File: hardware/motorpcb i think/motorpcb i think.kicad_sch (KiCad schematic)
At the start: 0 parts

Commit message: started schematic
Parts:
- added U1: PCA9685PW_Q900_118, symbol motorpcb i think:PCA9685PW_Q900_118

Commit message: continued schematic work
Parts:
- removed U1: PCA9685PW_Q900_118, symbol motorpcb i think:PCA9685PW_Q900_118
- added C1: 100nf, symbol Device:C
- added C2, C5: 10u, symbol Device:C
- added C3: 22u, symbol Device:C
- added C4: 100n, symbol Device:C
- added D1: RED, symbol Device:D
- added D2: GREEN, symbol Device:D
- added D3: BLUE, symbol Device:D
- added J1: USB_C_Receptacle_USB2.0_16P, symbol Connector:USB_C_Receptacle_USB2.0_16P
- added R1, R2, R3, R4, R5, R6: 5.1K, symbol Device:R
- added SW1, SW2: SW_Push, symbol Switch:SW_Push
- added U1: ESP32-S3-WROOM-1-N8, ESP32-S3-WROOM-1-N8:XCVR_ESP32-S3-WROOM-1-N8, symbol motorpcb i think:ESP32-S3-WROOM-1-N8
- added U2: LD1117S33TR, LD1117S33TR:SOT230P700X180-4N, symbol motorpcb i think:LD1117S33TR
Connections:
- new net: J1.A5 (CC1), R2.1
- new net: D1.2 (A), R3.2
- new net: J1.B5 (CC2), R1.1
- new net: D3.2 (A), R5.2
- new net: D2.2 (A), R4.2
- new net +3V3: C2.1, C3.1, C4.1, R4.1, R6.1, U1.2 (3V3), U2.2 (OUT), U2.4 (OUT)
- new net +5V: C1.1, J1.A4 (VBUS), J1.A9 (VBUS), J1.B4 (VBUS), J1.B9 (VBUS), R3.1, U2.3 (IN)
- new net D+: J1.A6 (D+), J1.B6 (D+), U1.14 (IO20)
- new net D-: J1.A7 (D-), J1.B7 (D-), U1.13 (IO19)
- new net GND: C1.2, C2.2, C3.2, C4.2, C5.2, D1.1 (K), D2.1 (K), D3.1 (K), J1.A1 (GND), J1.A12 (GND), J1.B1 (GND), J1.B12 (GND), J1.S1 (SHIELD), R1.2, R2.2, SW1.1, SW2.1, U1.1 (GND), U1.40 (GND), U1.41_1 (GND), U1.41_2 (GND), U1.41_3 (GND), U1.41_4 (GND), U1.41_5 (GND), U1.41_6 (GND), U1.41_7 (GND), U1.41_8 (GND), U1.41_9 (GND), U2.1 (GND)
- new net GPIO0: SW1.2, U1.27 (IO0)
- new net GPIO21: R5.1, U1.23 (IO21)
- new net en: C5.1, R6.2, SW2.2, U1.3 (EN)
- no-connect marks 0 -> 2
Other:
- note added: "boot / reset"
- note added: "esp32 3v3 regulator"
- note added: "indicator LED"
- note added: "usb c connector"

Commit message: finishing up basic esp32s3 hardware
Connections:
- net GPIO17: now reaches U1.10 (IO17)
- net GPIO18: now reaches U1.11 (IO18)
- net GPIO8: now reaches U1.12 (IO8)
- net GPIO3: now reaches U1.15 (IO3)
- net GPIO46: now reaches U1.16 (IO46)
- net GPIO9: now reaches U1.17 (IO9)
- net GPIO10: now reaches U1.18 (IO10)
- net GPIO11: now reaches U1.19 (IO11)
- net GPIO12: now reaches U1.20 (IO12)
- net GPIO13: now reaches U1.21 (IO13)
- net GPIO14: now reaches U1.22 (IO14)
- net GPIO47: now reaches U1.24 (IO47)
- net GPIO48: now reaches U1.25 (IO48)
- net GPIO45: now reaches U1.26 (IO45)
- net GPIO35: now reaches U1.28 (IO35)
- net GPIO36: now reaches U1.29 (IO36)
- net GPIO37: now reaches U1.30 (IO37)
- net GPIO38: now reaches U1.31 (IO38)
- net GPIO39: now reaches U1.32 (IO39)
- net GPIO40: now reaches U1.33 (IO40)
- net GPIO41: now reaches U1.34 (IO41)
- net GPIO42: now reaches U1.35 (IO42)
- net GPIO2: now reaches U1.38 (IO2)
- net GPIO1: now reaches U1.39 (IO1)
- net GPIO4: now reaches U1.4 (IO4)
- net GPIO5: now reaches U1.5 (IO5)
- net GPIO6: now reaches U1.6 (IO6)
- net GPIO7: now reaches U1.7 (IO7)
- net GPIO15: now reaches U1.8 (IO15)
- net GPIO16: now reaches U1.9 (IO16)
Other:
- note added: "3.3V regulator"
- note added: "boot / reset | gpio0, en"
- note added: "indicator LED | gpio 21"
- note removed: "boot / reset"
- note removed: "esp32 3v3 regulator"
- note removed: "indicator LED"
- moved on the sheet: U1

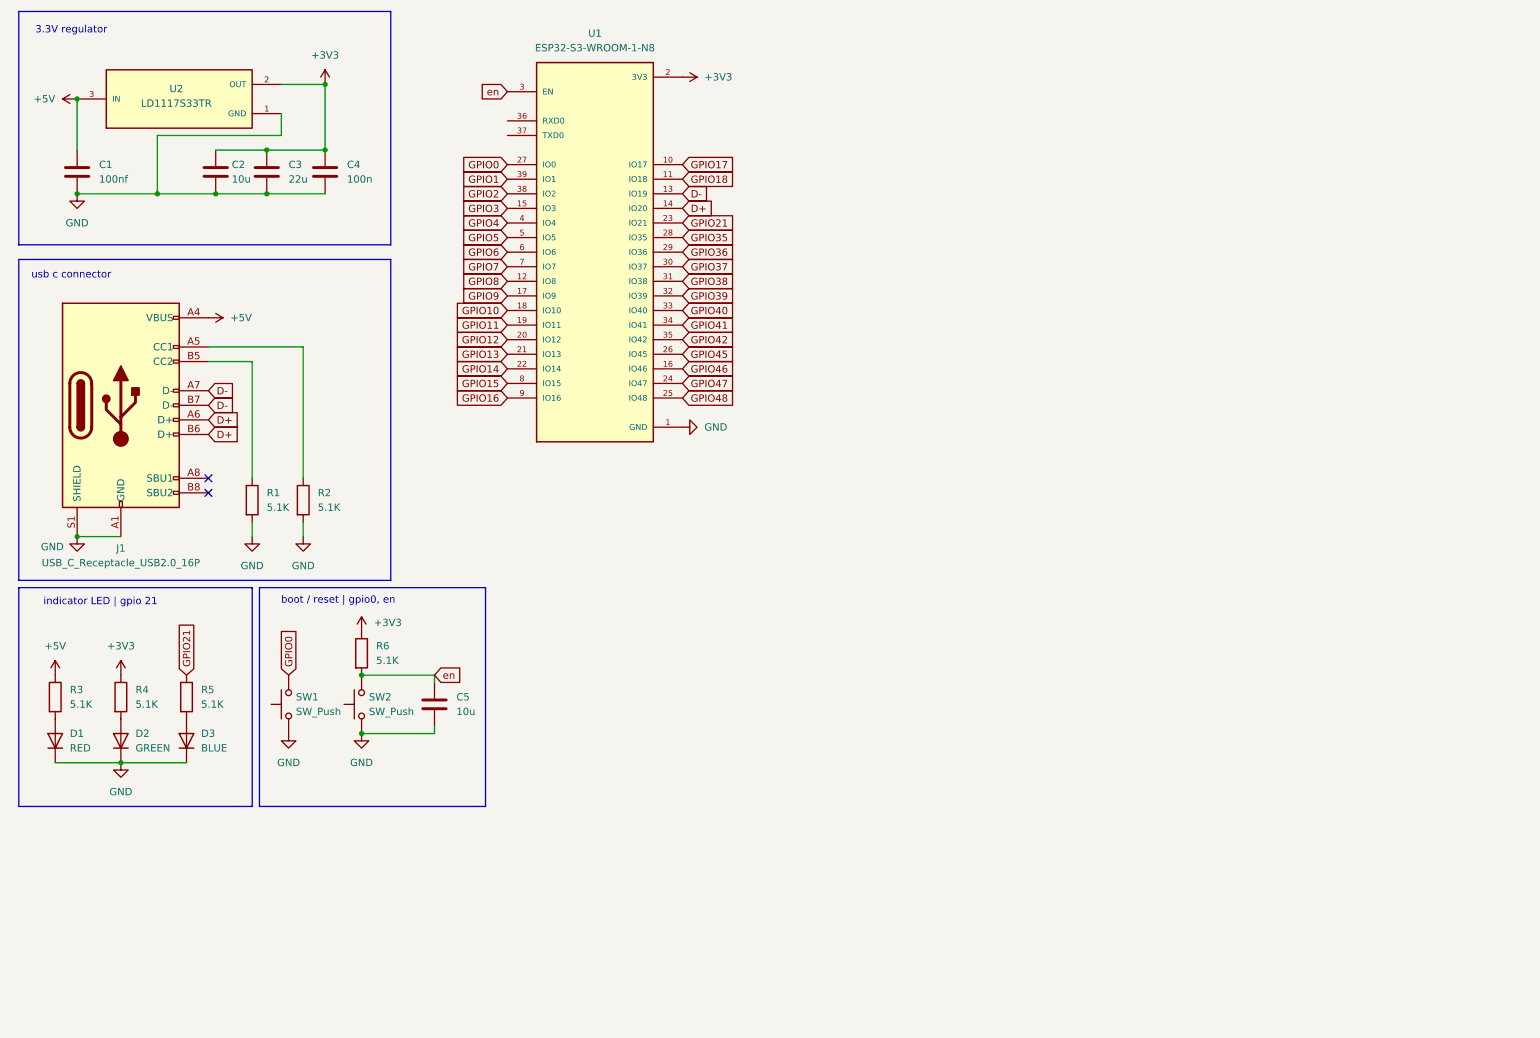
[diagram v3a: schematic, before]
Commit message: 12 -> 3.3 progress
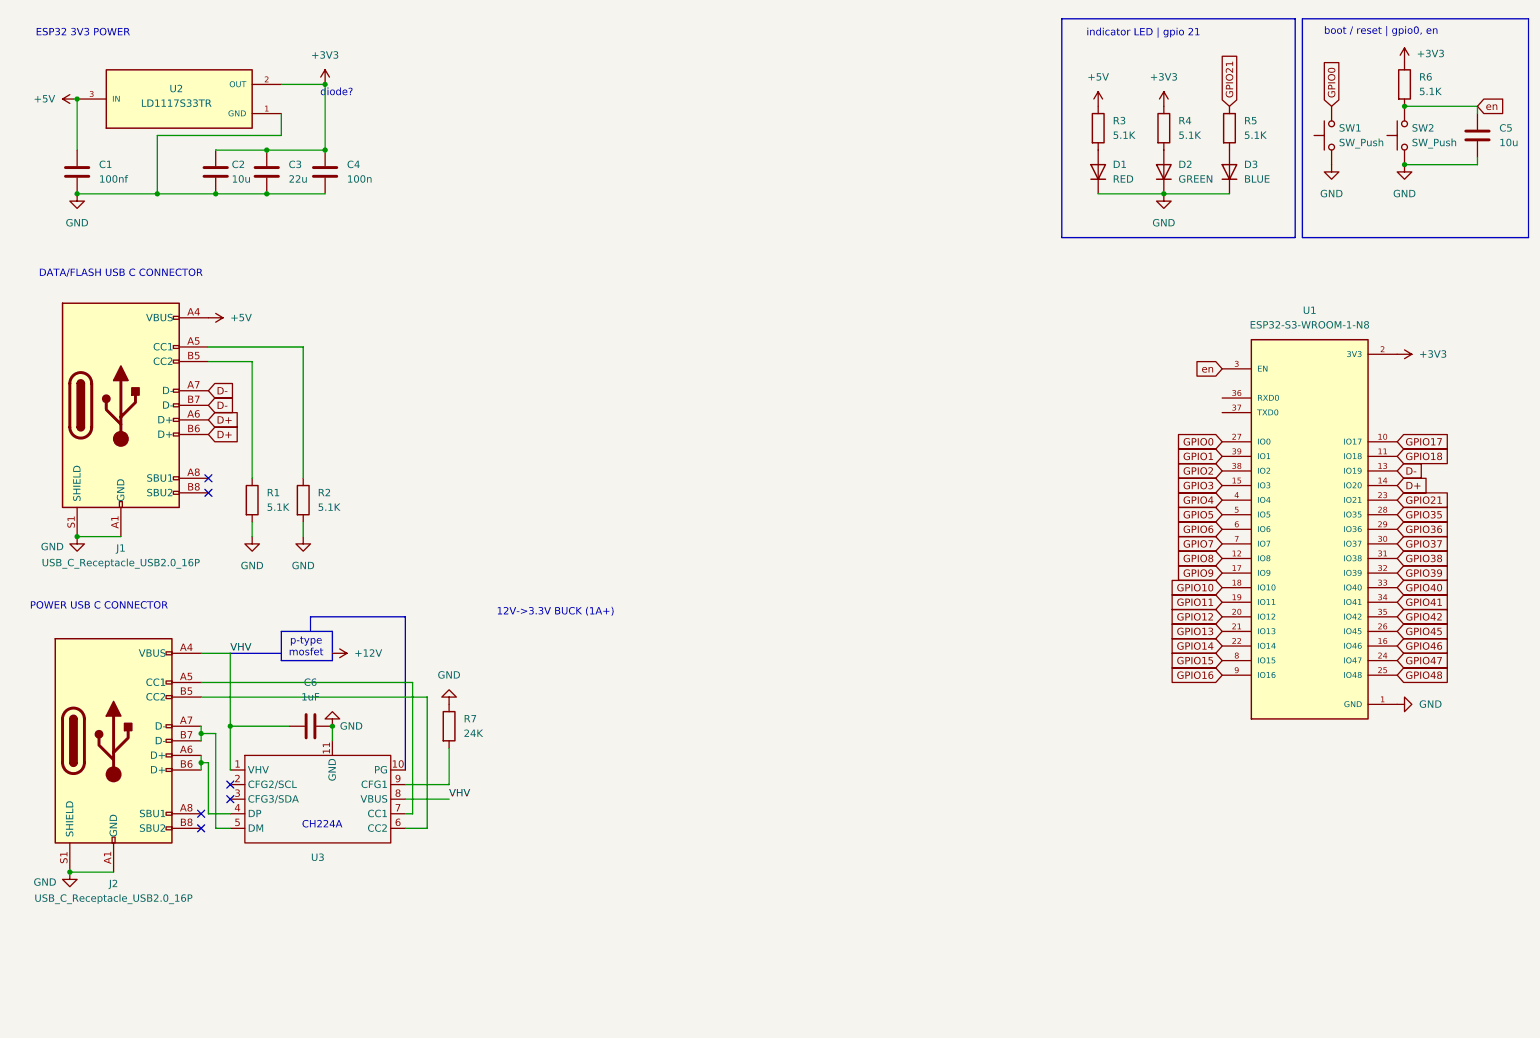
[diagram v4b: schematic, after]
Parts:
- added C6: 1uF, symbol Device:C
- added J2: USB_C_Receptacle_USB2.0_16P, symbol Connector:USB_C_Receptacle_USB2.0_16P
- added R7: 24K, symbol Device:R
- added U3: ~, ProLib_pcs_2025-12-27:ESSOP-10_L4.9-W3.9-P1.0-LS6.0-TL-EP, symbol motorpcb i think:CH224A
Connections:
- net GND: now also C6.2, J2.A1 (GND), J2.A12 (GND), J2.B1 (GND), J2.B12 (GND), J2.S1 (SHIELD), R7.1, U3.11 (GND)
- new net: J2.A5 (CC1), U3.7 (CC1)
- new net: J2.A6 (D+), J2.B6 (D+), U3.4 (DP)
- new net: J2.A7 (D-), J2.B7 (D-), U3.5 (DM)
- new net: J2.B5 (CC2), U3.6 (CC2)
- new net: R7.2, U3.9 (CFG1)
- new net VHV: C6.1, J2.A4 (VBUS), J2.A9 (VBUS), J2.B4 (VBUS), J2.B9 (VBUS), U3.1 (VHV), U3.8 (VBUS)
- no-connect marks 2 -> 6
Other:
- note added: "12V->3.3V BUCK (1A+)"
- note added: "CH224A"
- note added: "DATA/FLASH USB C CONNECTOR"
- note added: "ESP32 3V3 POWER"
- note added: "POWER USB C CONNECTOR"
- note added: "diode?"
- note added: "p-type mosfet"
- note removed: "3.3V regulator"
- note removed: "usb c connector"
- moved on the sheet: C5, D1, D2, D3, R3, R4, R5, R6, SW1, SW2, U1

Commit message: 12v -> 3.3v prog
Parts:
- added C10: 22nF, symbol Device:C
- added C7, C8: 10uF, symbol Device:C
- added C9: 0.1uF, symbol Device:C
- added L1: 6.8uH, symbol Device:L
- added R8: 191k, symbol Device:R
- added R9: 49.9k, symbol Device:R
- added U4: ~, MP2338GTLZ:SOT-583-8_L2.1-W1.2-P0.50-LS1.6-BR, symbol motorpcb i think:MP2338GTL-Z_C7210174
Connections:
- net +12V: now also C7.1, C8.1, C9.1, R8.1, U4.2 (VIN)
- net GND: now also C10.2, C7.2, C8.2, C9.2, R9.2, U4.4 (GND)
- net en renamed ENABLE
- new net: C10.1, U4.7 (SS)
- new net EN: R8.2, R9.1, U4.6 (EN)
- new net PG: U4.1 (PG)

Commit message: schematic near finish
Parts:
- removed C10: 22nF, symbol Device:C
- removed C7, C8: 10uF, symbol Device:C
- removed C9: 0.1uF, symbol Device:C
- removed L1: 6.8uH, symbol Device:L
- removed R2: 5.1K, symbol Device:R
- removed R8: 191k, symbol Device:R
- removed R9: 49.9k, symbol Device:R
- removed U4: ~, MP2338GTLZ:SOT-583-8_L2.1-W1.2-P0.50-LS1.6-BR, symbol motorpcb i think:MP2338GTL-Z_C7210174
- added C11: 10u, Capacitor_SMD:C_0603_1608Metric, symbol Device:C
- added C12: 22u, Capacitor_SMD:C_1206_3216Metric, symbol Device:C
- added C13: 100n, Capacitor_SMD:C_0402_1005Metric, symbol Device:C
- added C7: 10uF, Capacitor_SMD:C_0805_2012Metric, symbol Device:C_Polarized
- added D4: D, symbol Device:D
- added J10, J7, J8, J9: Conn_01x04_Pin, Connector_PinHeader_2.54mm:PinHeader_1x04_P2.54mm_Vertical, symbol Connector:Conn_01x04_Pin
- added J11: Conn_01x02_Pin, Connector_PinHeader_2.54mm:PinHeader_1x02_P2.54mm_Vertical, symbol Connector:Conn_01x02_Pin
- added J3, J6: Conn_01x15_Pin, Connector_PinHeader_2.54mm:PinHeader_1x15_P2.54mm_Vertical, symbol Connector:Conn_01x15_Pin
- added J4, J5: Screw_Terminal_01x02, TerminalBlock:TerminalBlock_MaiXu_MX126-5.0-02P_1x02_P5.00mm, symbol Connector:Screw_Terminal_01x02
- added U4: MP8040, motorpcb i think:MP8040, symbol motorpcb i think:MP8040DN
- BOOT1: renamed from SW1; footprint (none) -> Button_Switch_THT:SW_PUSH_6mm
- C1: footprint (none) -> Capacitor_SMD:C_0402_1005Metric
- C2: value 10u -> 47nF; footprint (none) -> Capacitor_SMD:C_0603_1608Metric
- C3: value 22u -> 1uF; footprint (none) -> Capacitor_SMD:C_0603_1608Metric
- C4: value 100n -> 0.1uF; footprint (none) -> Capacitor_SMD:C_0402_1005Metric
- C5, C6: footprint (none) -> Capacitor_SMD:C_0603_1608Metric
- D1, D2: footprint (none) -> Diode_SMD:D_0603_1608Metric
- D3: value BLUE -> GREEN; footprint (none) -> Diode_SMD:D_0603_1608Metric
- J1, J2: footprint (none) -> motorpcb i think:USB-C_SMD-TYPE-C-31-M-12_1
- R1: value 5.1K -> 27K; footprint (none) -> Resistor_SMD:R_0402_1005Metric
- R3: value 5.1K -> 10k; footprint (none) -> Resistor_SMD:R_0402_1005Metric
- R4, R5: value 5.1K -> 1.2K; footprint (none) -> Resistor_SMD:R_0402_1005Metric
- R6: value 5.1K -> 10K; footprint (none) -> Resistor_SMD:R_0402_1005Metric
- R7: footprint (none) -> Resistor_SMD:R_0603_1608Metric
- RESET1: renamed from SW2; footprint (none) -> Button_Switch_THT:SW_PUSH_6mm
- U1: footprint ESP32-S3-WROOM-1-N8:XCVR_ESP32-S3-WROOM-1-N8 -> motorpcb i think:XCVR_ESP32-S3-WROOM-1-N8
- U2: footprint LD1117S33TR:SOT230P700X180-4N -> motorpcb i think:LD11
- U3: footprint ProLib_pcs_2025-12-27:ESSOP-10_L4.9-W3.9-P1.0-LS6.0-TL-EP -> motorpcb i think:ch224a
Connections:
- net +12V: now also C1.1, C4.1, R3.1, U2.3 (IN), C7.1, D4.1 (K), J4.2 (Pin_2), U4.2 (SP)
- net +3V3: now also C11.1, C12.1, C13.1, J10.1 (Pin_1), J10.2 (Pin_2), J10.3 (Pin_3), J10.4 (Pin_4); no longer C2.1, C3.1, C4.1
- net GND: now also C11.2, C12.2, C13.2, C7.2, J4.1 (Pin_1), J5.1 (Pin_1), J8.1 (Pin_1), J8.2 (Pin_2), J8.3 (Pin_3), J8.4 (Pin_4), U4.4 (GND), U4.9 (EP); no longer C2.2, R1.2
- net GPIO1: now also J3.1 (Pin_1)
- net GPIO10: now also J3.10 (Pin_10)
- net GPIO11: now also J3.11 (Pin_11)
- net GPIO12: now also J3.12 (Pin_12)
- net GPIO13: now also J3.13 (Pin_13)
- net GPIO14: now also R1.1, J3.14 (Pin_14), U4.8 (FLT)
- net GPIO15: now also J3.15 (Pin_15), U4.6 (SHDN)
- net GPIO16: now also J6.1 (Pin_1), U4.1 (PWM)
- net GPIO17: now also J6.2 (Pin_2)
- net GPIO18: now also J6.3 (Pin_3)
- net GPIO2: now also J3.2 (Pin_2)
- net GPIO3: now also J3.3 (Pin_3)
- net GPIO35: now also J6.4 (Pin_4)
- net GPIO36: now also J6.5 (Pin_5)
- net GPIO37: now also J6.6 (Pin_6)
- net GPIO38: now also J6.7 (Pin_7)
- net GPIO39: now also J6.8 (Pin_8)
- net GPIO4: now also J3.4 (Pin_4)
- net GPIO40: now also J6.9 (Pin_9)
- net GPIO41: now also J6.10 (Pin_10)
- net GPIO42: now also J6.11 (Pin_11)
- net GPIO45: now also J6.12 (Pin_12)
- net GPIO46: now also J6.13 (Pin_13)
- net GPIO47: now also J6.14 (Pin_14)
- net GPIO48: now also J6.15 (Pin_15)
- net GPIO5: now also J3.5 (Pin_5)
- net GPIO6: now also J3.6 (Pin_6)
- net GPIO7: now also J3.7 (Pin_7)
- net GPIO8: now also J3.8 (Pin_8)
- net GPIO9: now also J3.9 (Pin_9)
- net VHV: now also D4.2 (A)
- net at J1.B5 (CC2): no longer R1.1
- net at U1.36 (RXD0): now also J11.1 (Pin_1)
- net at U1.37 (TXD0): now also J11.2 (Pin_2)
- net +5V: no longer names the net of J1.A4 (VBUS), J1.A9 (VBUS), J1.B4 (VBUS), J1.B9 (VBUS)
- net +5V: no longer C1.1, R3.1, U2.3 (IN)
- new net: C2.1, U4.5 (BS)
- new net: C3.1, R1.2, U4.7 (DRV)
- new net: J7.1 (Pin_1), J7.2 (Pin_2), J7.3 (Pin_3), J7.4 (Pin_4)
- new net: J9.1 (Pin_1), J9.2 (Pin_2), J9.3 (Pin_3), J9.4 (Pin_4)
- new net M+: C2.2, J5.2 (Pin_2), U4.3 (SW)
- no-connect marks 6 -> 10
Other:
- note added: "12v dc backup"
- note added: "3.3V RAIL"
- note added: "BREAKOUT PINS"
- note added: "MOTOR DRIVER"
- note added: "TERMINALS/EXTRA PROTOTYPE PINS"
- note added: "motor power"
- note removed: "12V->3.3V BUCK (1A+)"
- note removed: "ESP32 3V3 POWER"
- note removed: "diode?"
- note removed: "p-type mosfet"
- moved on the sheet: C1, C6, J1, J2, R7, U1, U2, U3

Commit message: schematic finished
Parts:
- removed D4: D, symbol Device:D
- added +3V3: TestPoint, TestPoint:TestPoint_Keystone_5010-5014_Multipurpose, symbol Connector:TestPoint
- added J12: Screw_Terminal_01x02, TerminalBlock:TerminalBlock_MaiXu_MX126-5.0-02P_1x02_P5.00mm, symbol Connector:Screw_Terminal_01x02
- added T1: GND, TestPoint:TestPoint_Keystone_5010-5014_Multipurpose, symbol Connector:TestPoint
- added T2: VHV, TestPoint:TestPoint_Keystone_5010-5014_Multipurpose, symbol Connector:TestPoint
- added T3: M+, TestPoint:TestPoint_Keystone_5010-5014_Multipurpose, symbol Connector:TestPoint
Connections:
- net +3V3: now also +3V3.1
- net GND: now also J12.1 (Pin_1), T1.1
- net M+: now also T3.1
- net VHV: now also J12.2 (Pin_2), T2.1
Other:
- note added: "12v entry"
- note removed: "12v dc backup"
